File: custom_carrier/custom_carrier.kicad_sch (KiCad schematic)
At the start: 16 parts, among them J1 ERF5-040-05.0-X-DV, J13 PJ-002AH-SMT-TR, J14 87832-1420, J2 ERF5-040-05.0-X-DV, J3 ERF5-040-05.0-X-DV, J4 ERF5-040-05.0-X-DV, J5 45230-220230, J6 45230-220230

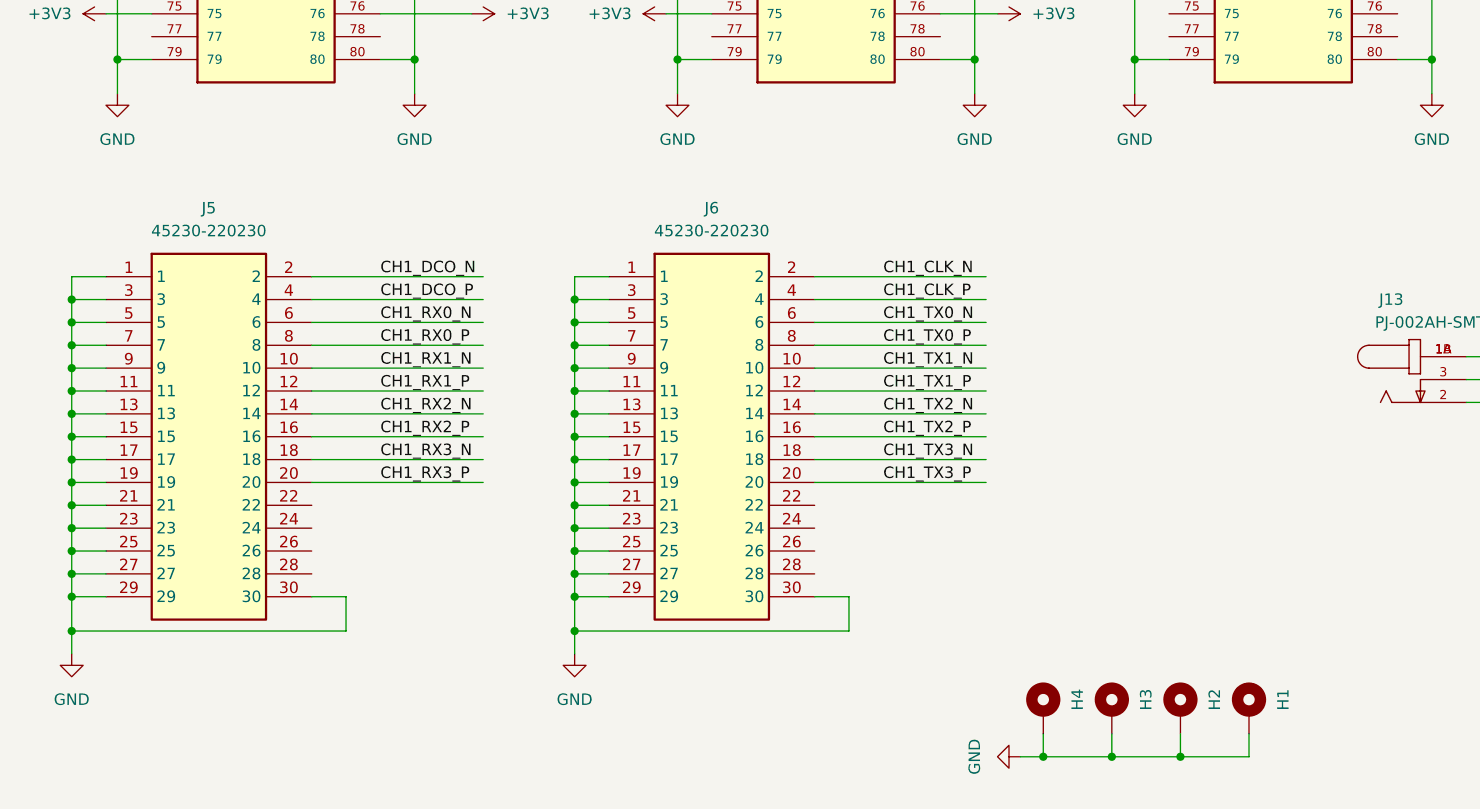
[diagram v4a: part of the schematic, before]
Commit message: rewired 3M connectors to recommended diff pair arrangement. tuned diff pair skews.
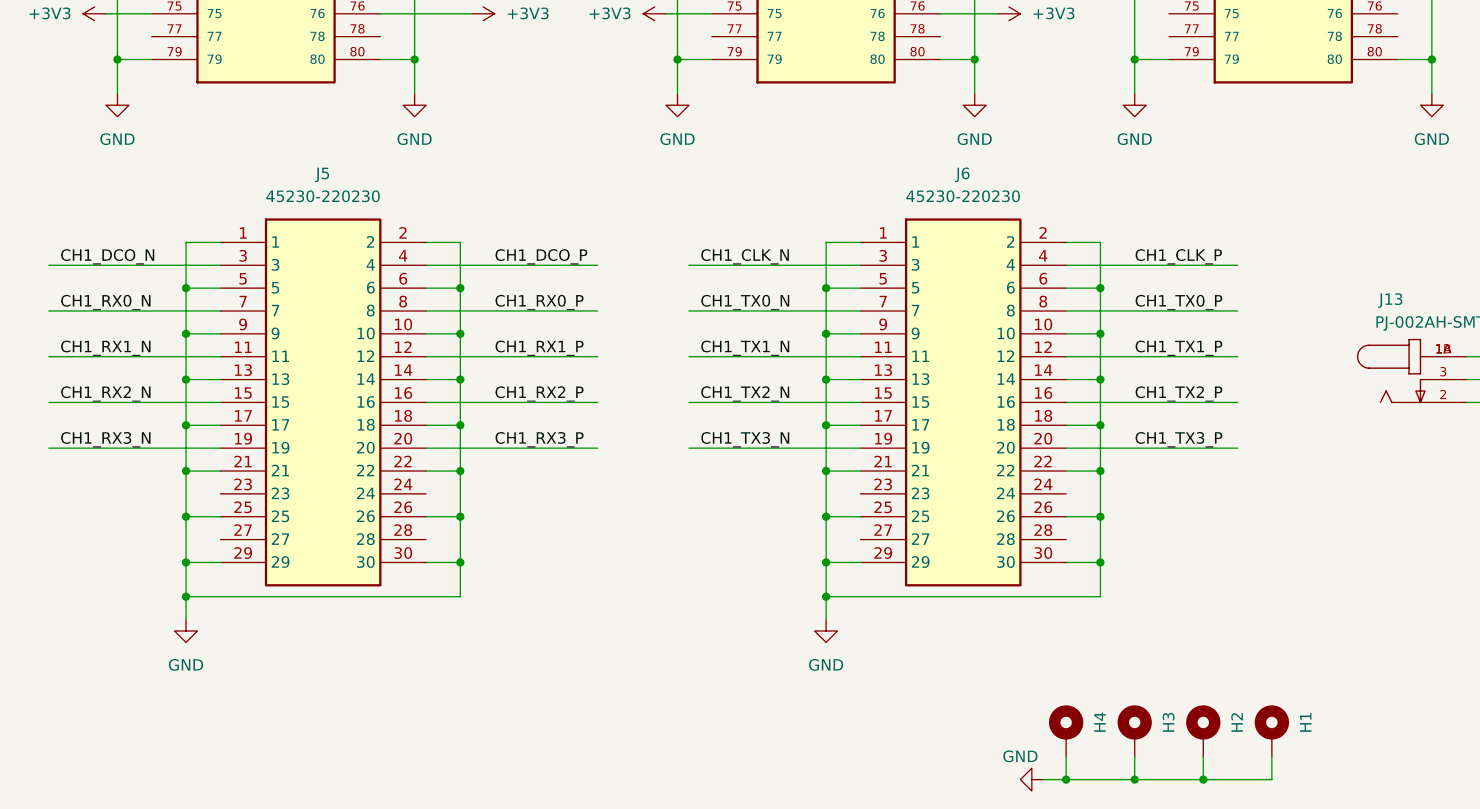
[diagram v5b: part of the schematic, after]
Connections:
- net CH1_CLK_N: now also J6.3; no longer J6.2
- net CH1_DCO_N: now also J5.3; no longer J5.2
- net CH1_RX0_N: now also J5.7; no longer J5.6
- net CH1_RX1_N: now also J5.11; no longer J5.10
- net CH1_RX2_N: now also J5.15; no longer J5.14
- net CH1_RX3_N: now also J5.19; no longer J5.18
- net CH1_TX0_N: now also J6.7; no longer J6.6
- net CH1_TX1_N: now also J6.11; no longer J6.10
- net CH1_TX2_N: now also J6.15; no longer J6.14
- net CH1_TX3_N: now also J6.19; no longer J6.18
- net GND: now also J5.10, J5.14, J5.18, J5.2, J5.22, J5.26, J5.6, J6.10, J6.14, J6.18, J6.2, J6.22, J6.26, J6.6; no longer J5.11, J5.15, J5.19, J5.23, J5.27, J5.3, J5.7, J6.11, J6.15, J6.19, J6.23, J6.27, J6.3, J6.7
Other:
- moved on the sheet: H1, H2, H3, H4, J5, J6
